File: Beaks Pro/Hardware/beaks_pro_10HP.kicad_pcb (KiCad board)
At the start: 2 copper layers, 107.7 x 108.5 mm, 124 parts, among them J1 Pins_02x10_P2.54mm_TH, J11 out1, J12 out2, J13 Eurorack Power, J14 Pins_02x10_P2.54mm_TH, J2 Pins_02x10_P2.54mm_TH, J3 CV1, J4 CV2, J5 CV3, J6 CV4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

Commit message: Back PCB Done
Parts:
- moved D7 6.88 mm to (56.6, 66.1)
- moved D6 6.76 mm to (56.6, 59.3)
- moved D5 0.76 mm to (56.6, 52.3)
- moved D4 0.70 mm to (56.6, 45.6)
- moved C9 0.62 mm to (136.7, 100.2)
- moved D3 0.50 mm to (56.6, 84.0)
- moved SW3 0.49 mm to (55.6, 77.8)
- moved SW2 0.36 mm to (55.6, 95.4)
- moved RV5 0.32 mm to (73.3, 65.7)
- moved R51 0.29 mm to (107.8, 78.5)
- moved RV2 0.24 mm to (38.2, 65.7)
- moved RV6 0.23 mm to (73.3, 80.8)
- moved J11 0.22 mm to (40.9, 125.6)
- moved J3 0.22 mm to (40.9, 125.6)
- moved R48 0.21 mm to (104.7, 93.2)
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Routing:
- net GND: track 0.00 -> 249.7 mm, vias 0 -> 7
- net -12V: track 0.00 -> 163.5 mm, vias 0 -> 2
- net +12V: track 0.00 -> 162.3 mm, vias 0 -> 4
- net +3V3: track 0.00 -> 119.1 mm, vias 0 -> 1
- net Net-(U4B--): track 0.00 -> 114.6 mm, vias 0 -> 2
- net Net-(U4A--): track 0.00 -> 108.4 mm, vias 0 -> 5
- net /SW_TRIG1: track 0.00 -> 103.2 mm, vias 0 -> 4
- net /LED_SALIDA_1: track 0.00 -> 97.2 mm, vias 0 -> 1
- net /Inputs/CV4: track 0.00 -> 92.2 mm, vias 0 -> 6
- net /LED2: track 0.00 -> 83.2 mm, vias 0 -> 1
- net /LED_SALIDA_2: track 0.00 -> 82.5 mm, vias 0 -> 1
- net /TRIG_2: track 0.00 -> 81.0 mm, vias 0 -> 3
- net /LED5: track 0.00 -> 79.1 mm, vias 0 -> 3
- net Net-(U5D--): track 0.00 -> 74.7 mm, vias 0 -> 5
- net /SW_TRIG2: track 0.00 -> 74.5 mm, vias 0 -> 1
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- added copper zone on B.Cu, net GND

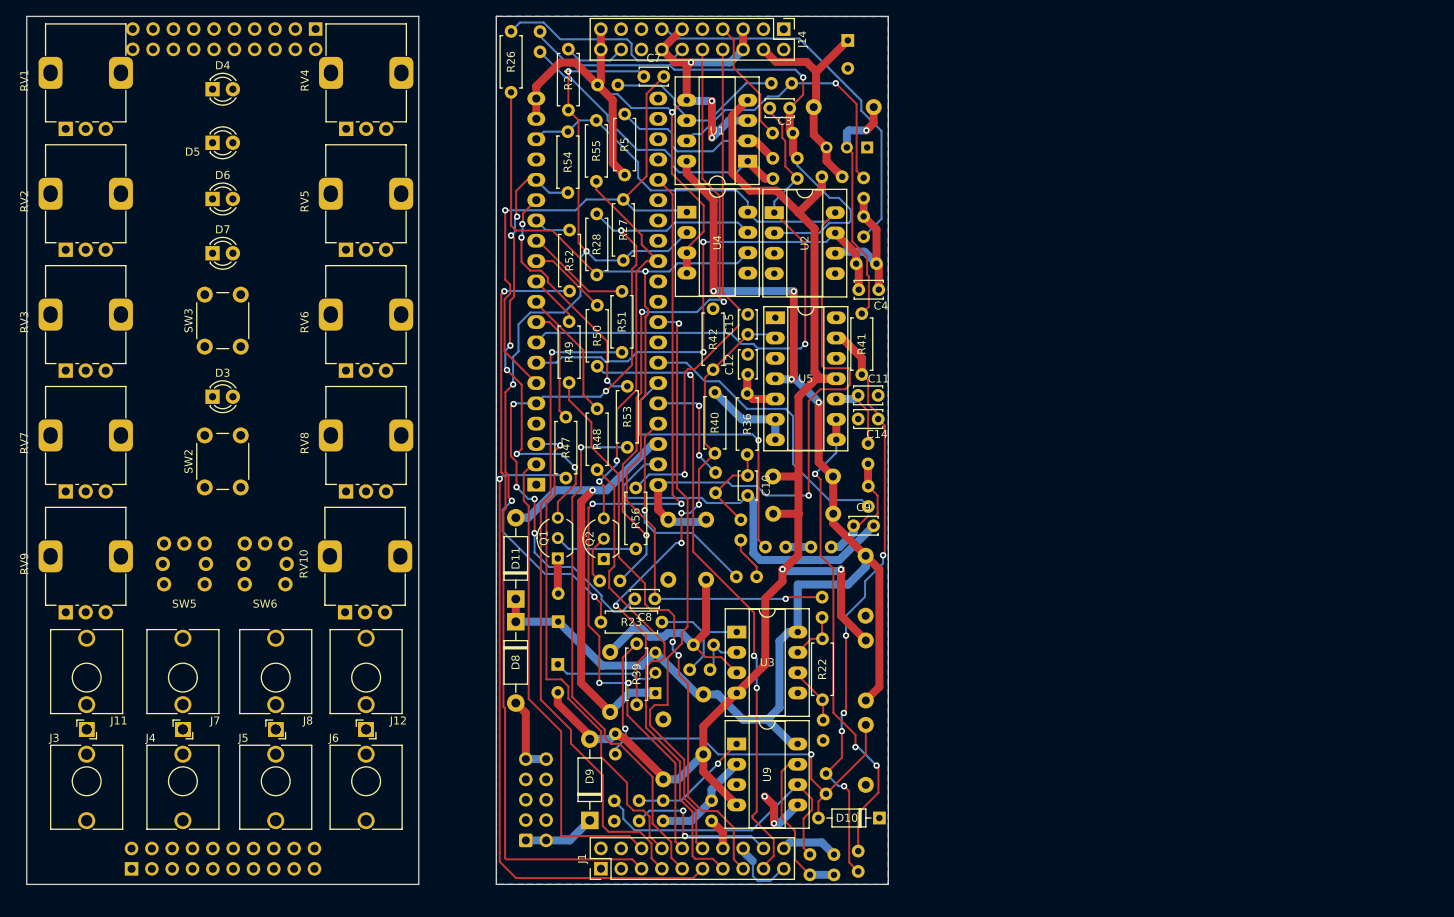
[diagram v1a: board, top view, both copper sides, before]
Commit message: Increased via spacing to a minimum of 0.25mm
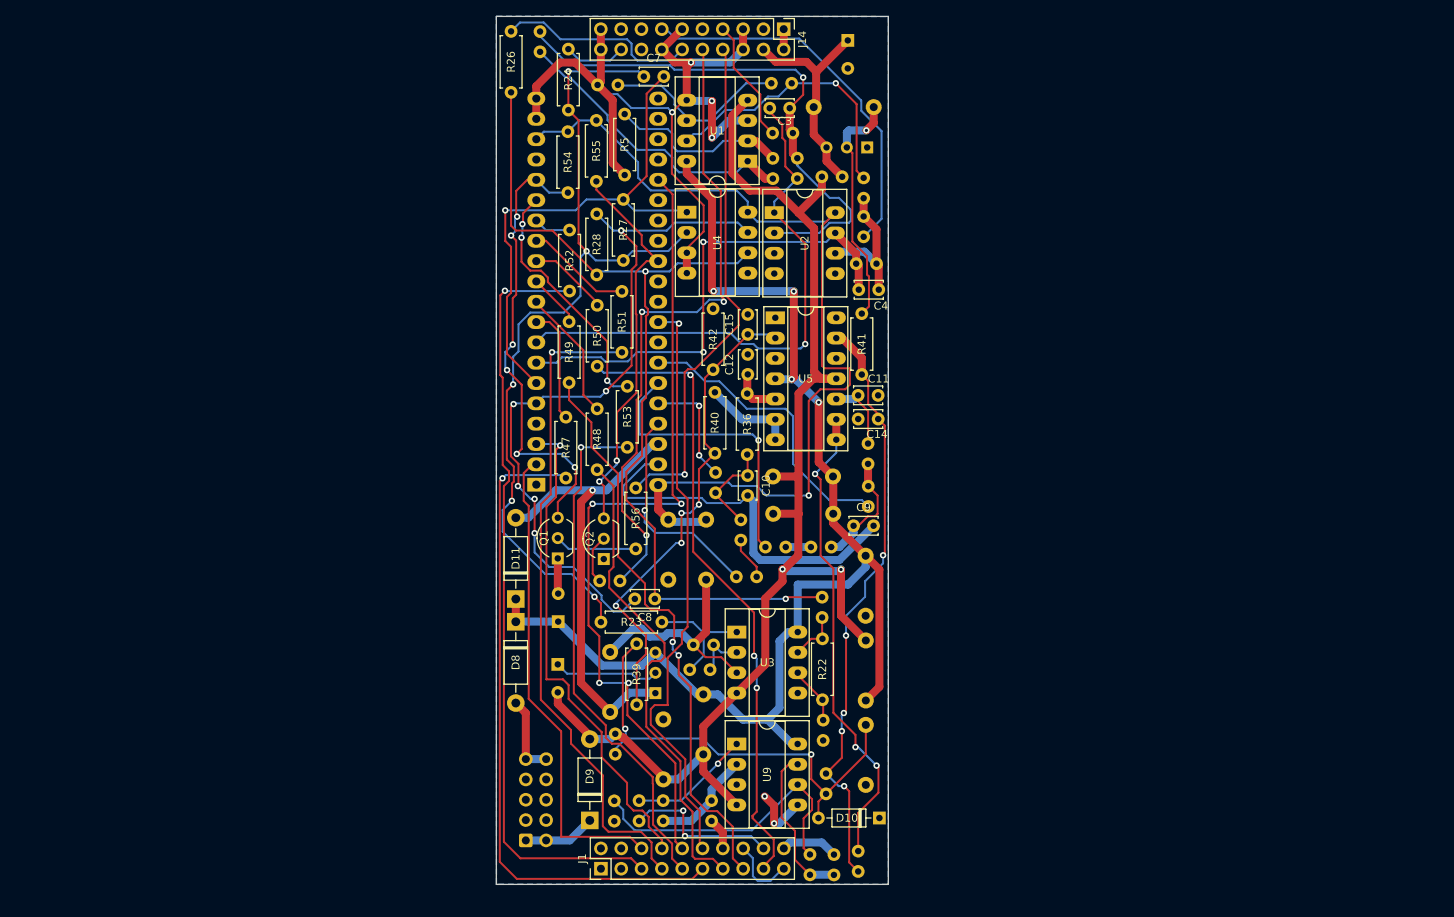
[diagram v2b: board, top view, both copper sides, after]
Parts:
- removed D3, D4, D5, D6, D7: LED, LED_THT:LED_D3.0mm
- removed J11: out1, Library:Jack_3.5mm_QingPu_WQP-PJ398SM_Vertical_CircularHoles_3D
- removed J12: out2, Library:Jack_3.5mm_QingPu_WQP-PJ398SM_Vertical_CircularHoles_3D
- removed J2, J9: Pins_02x10_P2.54mm_TH, Connector_PinSocket_2.54mm:PinSocket_2x10_P2.54mm_Vertical
- removed J3: CV1, Library:Jack_3.5mm_QingPu_WQP-PJ398SM_Vertical_CircularHoles_3D
- removed J4: CV2, Library:Jack_3.5mm_QingPu_WQP-PJ398SM_Vertical_CircularHoles_3D
- removed J5: CV3, Library:Jack_3.5mm_QingPu_WQP-PJ398SM_Vertical_CircularHoles_3D
- removed J6: CV4, Library:Jack_3.5mm_QingPu_WQP-PJ398SM_Vertical_CircularHoles_3D
- removed J7: in1, Library:Jack_3.5mm_QingPu_WQP-PJ398SM_Vertical_CircularHoles_3D
- removed J8: in2, Library:Jack_3.5mm_QingPu_WQP-PJ398SM_Vertical_CircularHoles_3D
- removed RV1, RV2, RV3, RV7: B10k, Library:Potentiometer_Alps_RK09K_Single_Vertical_DSHAFT
- removed RV10, RV4, RV5, RV6, RV8, RV9: B100k, Library:Potentiometer_Alps_RK09K_Single_Vertical
- removed SW2: SW_Dual, Button_Switch_THT:SW_PUSH_6mm_H13mm
- removed SW3: SW_Mode, Button_Switch_THT:SW_PUSH_6mm_H13mm
- removed SW5, SW6: SW_ML6, Library:ML6-H2T2GQA
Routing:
- net GND: track 249.7 -> 252.6 mm
- net /LED_SALIDA_1: track 97.2 -> 96.5 mm
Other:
- board size 107.7 x 108.5 mm -> 49 x 108.5 mm

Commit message: Update beaks_pro_10HP.kicad_pcb
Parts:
- added D3: LED, LED_THT:LED_D3.0mm, F.Cu at (96.7, 86.1)
- added D4: LED, LED_THT:LED_D3.0mm, F.Cu at (96.7, 47.6)
- added D5: LED, LED_THT:LED_D3.0mm, F.Cu at (96.7, 54.3)
- added D6: LED, LED_THT:LED_D3.0mm, F.Cu at (96.7, 61.4)
- added D7: LED, LED_THT:LED_D3.0mm, F.Cu at (96.7, 68.2)
- added J11: out1, Library:Jack_3.5mm_QingPu_WQP-PJ398SM_Vertical_CircularHoles_3D, F.Cu at (80.9, 127.7)
- added J12: out2, Library:Jack_3.5mm_QingPu_WQP-PJ398SM_Vertical_CircularHoles_3D, F.Cu at (115.9, 127.7)
- added J2: Pins_02x10_P2.54mm_TH, Connector_PinSocket_2.54mm:PinSocket_2x10_P2.54mm_Vertical, B.Cu at (109.5, 40.1)
- added J3: CV1, Library:Jack_3.5mm_QingPu_WQP-PJ398SM_Vertical_CircularHoles_3D, F.Cu at (80.9, 127.7)
- added J4: CV2, Library:Jack_3.5mm_QingPu_WQP-PJ398SM_Vertical_CircularHoles_3D, F.Cu at (93.0, 127.7)
- added J5: CV3, Library:Jack_3.5mm_QingPu_WQP-PJ398SM_Vertical_CircularHoles_3D, F.Cu at (104.6, 127.7)
- added J6: CV4, Library:Jack_3.5mm_QingPu_WQP-PJ398SM_Vertical_CircularHoles_3D, F.Cu at (115.9, 127.7)
- added J7: in1, Library:Jack_3.5mm_QingPu_WQP-PJ398SM_Vertical_CircularHoles_3D, F.Cu at (93.0, 127.7)
- added J8: in2, Library:Jack_3.5mm_QingPu_WQP-PJ398SM_Vertical_CircularHoles_3D, F.Cu at (104.6, 127.7)
- added J9: Pins_02x10_P2.54mm_TH, Connector_PinSocket_2.54mm:PinSocket_2x10_P2.54mm_Vertical, B.Cu at (86.5, 145.1)
- added RV1: B10k, Library:Potentiometer_Alps_RK09K_Single_Vertical_DSHAFT, F.Cu at (78.3, 52.6)
- added RV10: B100k, Library:Potentiometer_Alps_RK09K_Single_Vertical, F.Cu at (113.2, 113.0)
- added RV2: B10k, Library:Potentiometer_Alps_RK09K_Single_Vertical_DSHAFT, F.Cu at (78.3, 67.7)
- added RV3: B10k, Library:Potentiometer_Alps_RK09K_Single_Vertical_DSHAFT, F.Cu at (78.3, 82.8)
- added RV4: B100k, Library:Potentiometer_Alps_RK09K_Single_Vertical, F.Cu at (113.4, 52.6)
- added RV5: B100k, Library:Potentiometer_Alps_RK09K_Single_Vertical, F.Cu at (113.3, 67.7)
- added RV6: B100k, Library:Potentiometer_Alps_RK09K_Single_Vertical, F.Cu at (113.3, 82.8)
- added RV7: B10k, Library:Potentiometer_Alps_RK09K_Single_Vertical_DSHAFT, F.Cu at (78.3, 97.9)
- added RV8: B100k, Library:Potentiometer_Alps_RK09K_Single_Vertical, F.Cu at (113.3, 97.9)
- added RV9: B100k, Library:Potentiometer_Alps_RK09K_Single_Vertical, F.Cu at (78.3, 113.0)
- added SW2: SW_Dual, Button_Switch_THT:SW_PUSH_6mm_H13mm, F.Cu at (95.7, 97.4)
- added SW3: SW_Mode, Button_Switch_THT:SW_PUSH_6mm_H13mm, F.Cu at (95.7, 79.8)
- added SW5: SW_ML6, Library:ML6-H2T2GQA, F.Cu at (93.1, 107.0)
- added SW6: SW_ML6, Library:ML6-H2T2GQA, F.Cu at (103.2, 107.0)
- moved C11 68.2 mm to (205.5, 85.8)
- moved C21 68.2 mm to (206.4, 105.8)
- moved D10 68.2 mm to (208.1, 138.6)
- moved R11 68.2 mm to (206.2, 58.6)
- moved R12 68.2 mm to (206.2, 65.9)
- moved R20 68.2 mm to (201.1, 128.9)
- moved R25 68.2 mm to (201.0, 113.5)
- moved R45 68.2 mm to (201.0, 58.4)
- moved U6 68.2 mm to (206.6, 54.8)
- moved C10 68.2 mm to (191.7, 95.8)
- moved C18 68.2 mm to (168.0, 114.0)
- moved C23 68.2 mm to (174.5, 125.3)
- moved C6 68.2 mm to (186.5, 101.3)
- moved J1 68.2 mm to (173.3, 144.9)
- moved J14 68.2 mm to (196.2, 40.0)
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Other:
- board size 49 x 108.5 mm -> 135.8 x 108.6 mm
